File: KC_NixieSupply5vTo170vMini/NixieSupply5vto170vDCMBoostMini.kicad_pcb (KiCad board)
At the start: 2 copper layers, 38.6 x 29 mm, 40 parts, among them J1 Screw_Terminal_01x04, J2 CONN_01X01, J3 CONN_01X01, J4 CONN_01X01, J5 CONN_01X01, P1 USB_OTG, Q1 FDS2672CT, Q26 MMBTA42, U1 UCC3803

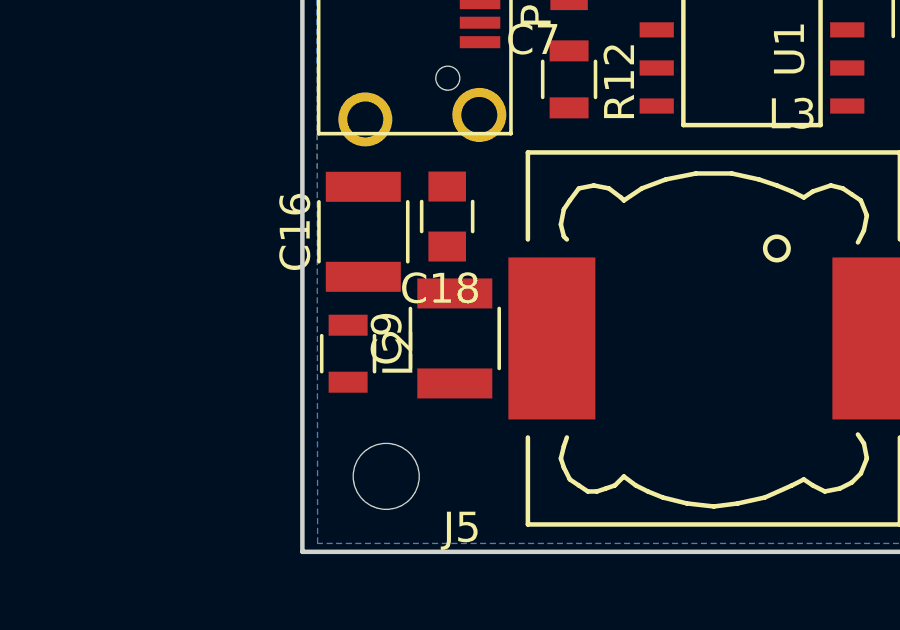
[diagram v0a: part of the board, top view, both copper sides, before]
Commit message: started layout and fixed netclass for the high current 5v input
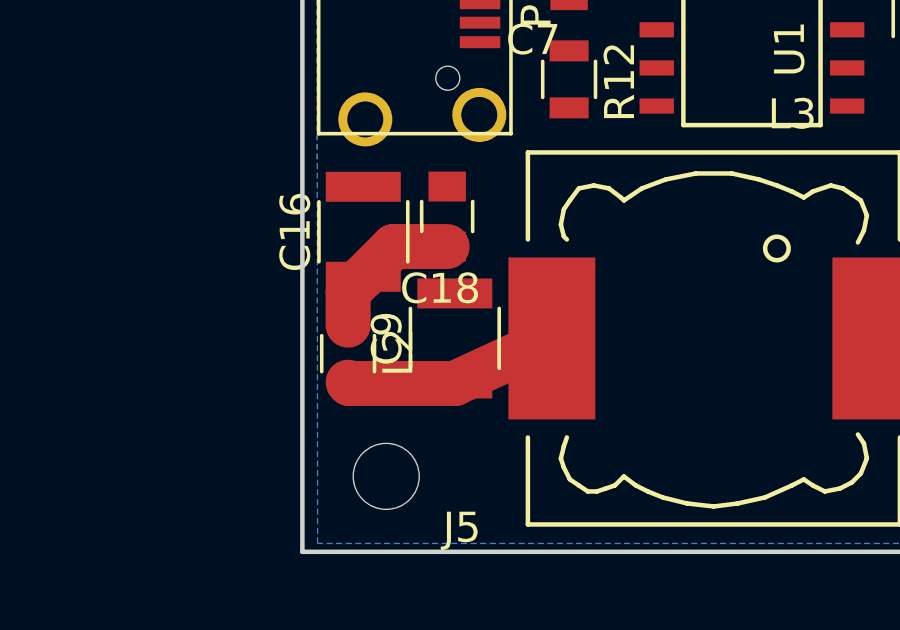
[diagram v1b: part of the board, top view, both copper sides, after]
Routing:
- net Net-(C9-Pad1): track 0.00 -> 7.14 mm
- net 5v_Power: track 0.00 -> 5.04 mm
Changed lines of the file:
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@@
   (general
     (links 77)
-    (no_connects 77)
-    (area 135.814999 81.966999 174.573001 111.073001)
+    (no_connects 73)
+    (area 17.081499 79.73792 229.894856 177.128)
     (thickness 1.6)
     (drawings 7)
-    (tracks 1)
+    (tracks 9)
     (zones 0)
     (modules 40)
@@
   )
   (setup
-    (last_trace_width 0.381)
+    (last_trace_width 1)
     (user_trace_width 0.2)
     (user_trace_width 0.4)
@@
     (mod_text_size 1 1)
     (mod_text_width 0.15)
-    (pad_size 1.143 1.143)
-    (pad_drill 0.635)
+    (pad_size 2.9 5.4)
+    (pad_drill 0)
     (pad_to_mask_clearance 0.0508)
     (aux_axis_origin 136.0932 73.1774)
@@
     (add_net "Net-(C6-Pad2)")
     (add_net "Net-(C7-Pad1)")
-    (add_net "Net-(C9-Pad1)")
     (add_net "Net-(J4-Pad1)")
     (add_net "Net-(J5-Pad1)")
@@
     (uvia_drill 0.3302)
     (add_net 5v_Power)
+    (add_net "Net-(C9-Pad1)")
     (add_net "Net-(Q1-Pad1)")
     (add_net "Net-(Q1-Pad4)")
@@
   )
   (segment (start 17.526 143.2633) (end 17.526 142.9893) (width 0.381) (layer F.Cu) (net 0))
+  (segment (start 140.716 100.822) (end 138.93 100.822) (width 1.5) (layer F.Cu) (net 10) (status 400000))
+  (segment (start 138.93 100.822) (end 137.922 101.83) (width 1.5) (layer F.Cu) (net 10) (status 800000))
+  (segment (start 137.414 103.444) (end 137.414 102.338) (width 1.5) (layer F.Cu) (net 10) (status 400000))
+  (segment (start 137.414 102.338) (end 137.922 101.83) (width 1.5) (layer F.Cu) (net 10) (status 800000))
+  (segment (start 140.97 105.386) (end 137.456 105.386) (width 1.5) (layer F.Cu) (net 20) (status C00000))
+  (segment (start 137.456 105.386) (end 137.414 105.344) (width 1.5) (layer F.Cu) (net 20) (status C00000))
+  (segment (start 144.206 103.886) (end 144.206 103.886) (width 1.5) (layer F.Cu) (net 20) (status C00000))
+  (segment (start 144.206 103.886) (end 140.97 105.386) (width 1.5) (layer F.Cu) (net 20) (status C00000))
   (zone (net 1) (net_name GND) (layer B.Cu) (hatch edge 0.508)
     (connect_pads (clearance 0.2))

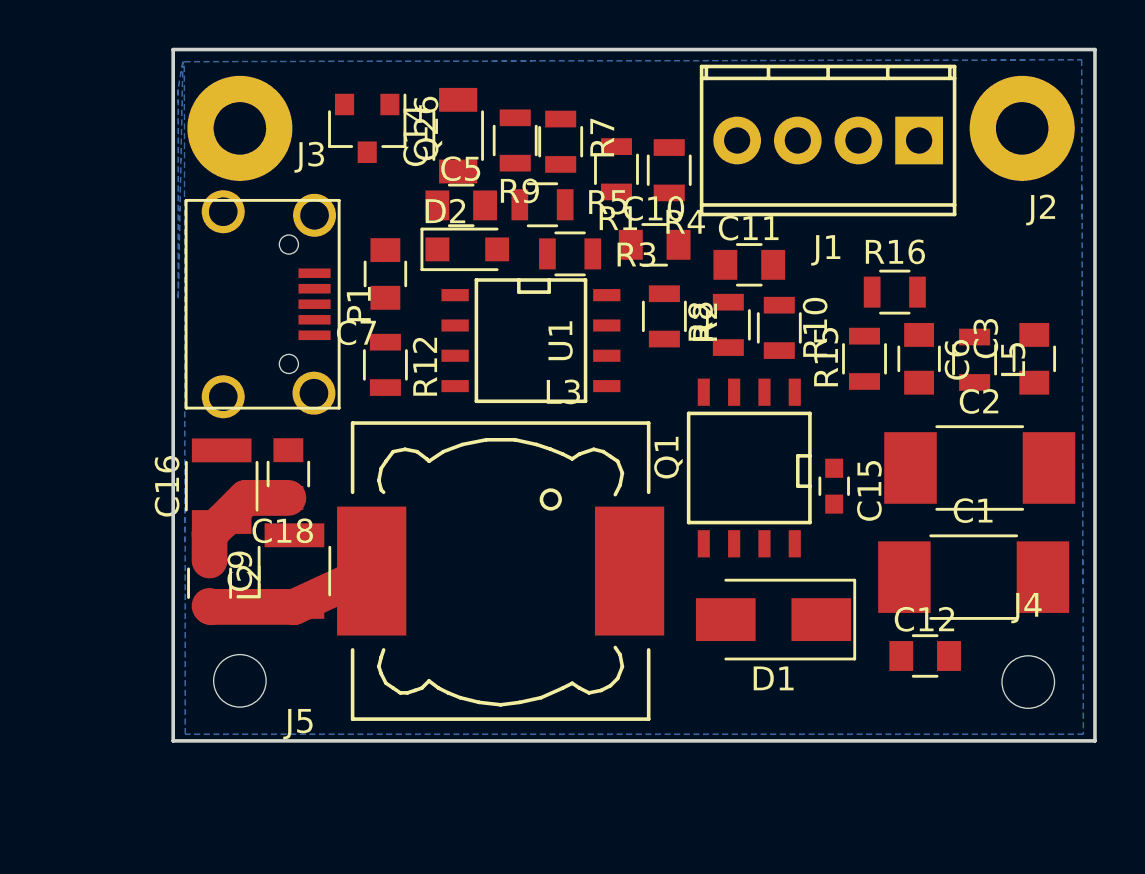
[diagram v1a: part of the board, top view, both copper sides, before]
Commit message: Finished the Gerber file for Mini Layout.   Need to add OSHW logo to bottom.
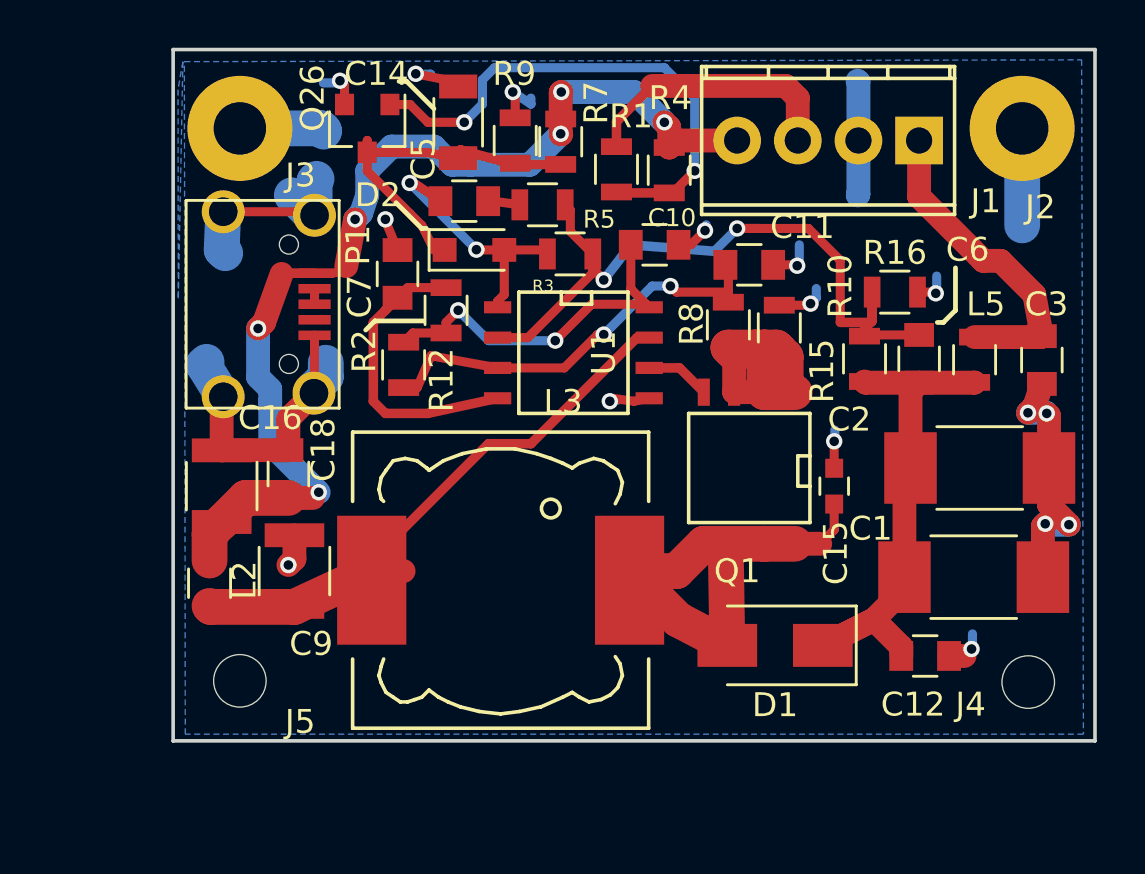
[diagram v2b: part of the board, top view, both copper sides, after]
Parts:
- moved R2 9.15 mm to (147.3, 93.0), turned to 270 degrees
- moved U1 1.85 mm to (152.7, 94.7)
- moved D1 1.08 mm to (161.1, 107.0)
- moved R12 0.76 mm to (145.5, 95.2)
- moved C14 0.56 mm to (147.8, 85.1)
- moved C7 0.51 mm to (145.3, 91.4)
- moved L3 0.38 mm to (149.6, 104.3)
- moved C3 0.32 mm to (172.3, 95.0)
- moved D2 0.30 mm to (148.5, 90.4)
- moved C5 0.22 mm to (148.1, 88.4)
- turned R4 to 90 degrees
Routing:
- net GND: track 0.00 -> 67.6 mm, vias 0 -> 16
- net 5v_Power: track 5.04 -> 45.3 mm, vias 0 -> 6
- net Net-(C6-Pad2): track 0.00 -> 31.6 mm, vias 0 -> 2
- net Net-(C1-Pad1): track 0.00 -> 22.1 mm
- net Net-(Q26-Pad1): track 0.00 -> 21.9 mm, vias 0 -> 2
- net Net-(C15-Pad1): track 0.00 -> 20.0 mm
- net Net-(C11-Pad1): track 0.00 -> 17.7 mm, vias 0 -> 2
- net Net-(C9-Pad1): track 7.14 -> 24.4 mm
- net Net-(C10-Pad1): track 0.00 -> 15.2 mm, vias 0 -> 2
- net Net-(C14-Pad1): track 0.00 -> 15.1 mm
- net +160V: track 0.00 -> 13.5 mm
- net Net-(C7-Pad1): track 0.00 -> 12.4 mm
- net N_ENABLE: track 0.00 -> 11.2 mm
- net Net-(Q1-Pad1): track 0.00 -> 11.1 mm
- net Net-(C5-Pad1): track 0.00 -> 11.1 mm, vias 0 -> 2
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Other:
- net class Default: clearance 0.254 -> 0.14
- net class Low Power Low Voltage: via_dia 685.8 -> 0.6858
- net class Power Low Voltage 2A 50v: clearance 0.254 -> 0.13
- rule trace_clearance: 0.254 -> 0.14

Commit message: Updated the copyright information to Mark Smith and added www.surfncircuits.com to Boards Also added a part number and date code.    yyww (last two digits of year and ww is the work week) NixieSupply Rev2_1804 NixieSupplyMini Rev1_1804
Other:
- board text added: "Mark Smith"
- board text added: "NixieSupplyMini Rev1_1804"
- board text added: "copyright (c) 2018"
- board text added: "www.surfncircuits.com"
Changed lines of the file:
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@@
     (links 77)
     (no_connects 0)
-    (area 135.814999 81.966999 174.573001 111.073001)
+    (area 17.195499 79.73792 229.894856 177.128)
     (thickness 1.6)
-    (drawings 16)
+    (drawings 20)
     (tracks 320)
     (zones 0)
@@
     )
   )
+  (gr_text "Mark Smith" (at 151.4475 109.0295) (layer B.SilkS)
+    (effects (font (size 1.5 1.5) (thickness 0.3)) (justify mirror))
+  )
+  (gr_text "copyright (c) 2018" (at 151.892 106.426) (layer B.SilkS)
+    (effects (font (size 1.5 1.5) (thickness 0.3)) (justify mirror))
+  )
+  (gr_text www.surfncircuits.com (at 154.4955 103.759) (layer B.SilkS)
+    (effects (font (size 1 1.5) (thickness 0.2)) (justify mirror))
+  )
+  (gr_text "NixieSupplyMini Rev1_1804" (at 155.448 98.8695) (layer B.SilkS)
+    (effects (font (size 1.5 1.5) (thickness 0.3)) (justify mirror))
+  )
   (gr_line (start 145.669 83.3755) (end 145.3515 83.3755) (angle 90) (layer F.SilkS) (width 0.2))

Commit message: Added OSHW_LOGO and the copyright symbol to both Files.    Also updated the gerber files and finished the Mini layout solution.
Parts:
- added G***: LOGO, LOGO, B.Cu at (159.7, 108.5)
- added G***: OSHW_logo_silkscreen-front_5mm, OSHW_logo_silkscreen-front_5mm, B.Cu at (150.4, 102.3)
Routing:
- net GND: track 67.6 -> 111.5 mm
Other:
- board text added: "Mark Smith 2018"
- board text removed: "Mark Smith"
- board text removed: "copyright (c) 2018"
